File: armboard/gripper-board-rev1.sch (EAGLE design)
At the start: 8 parts

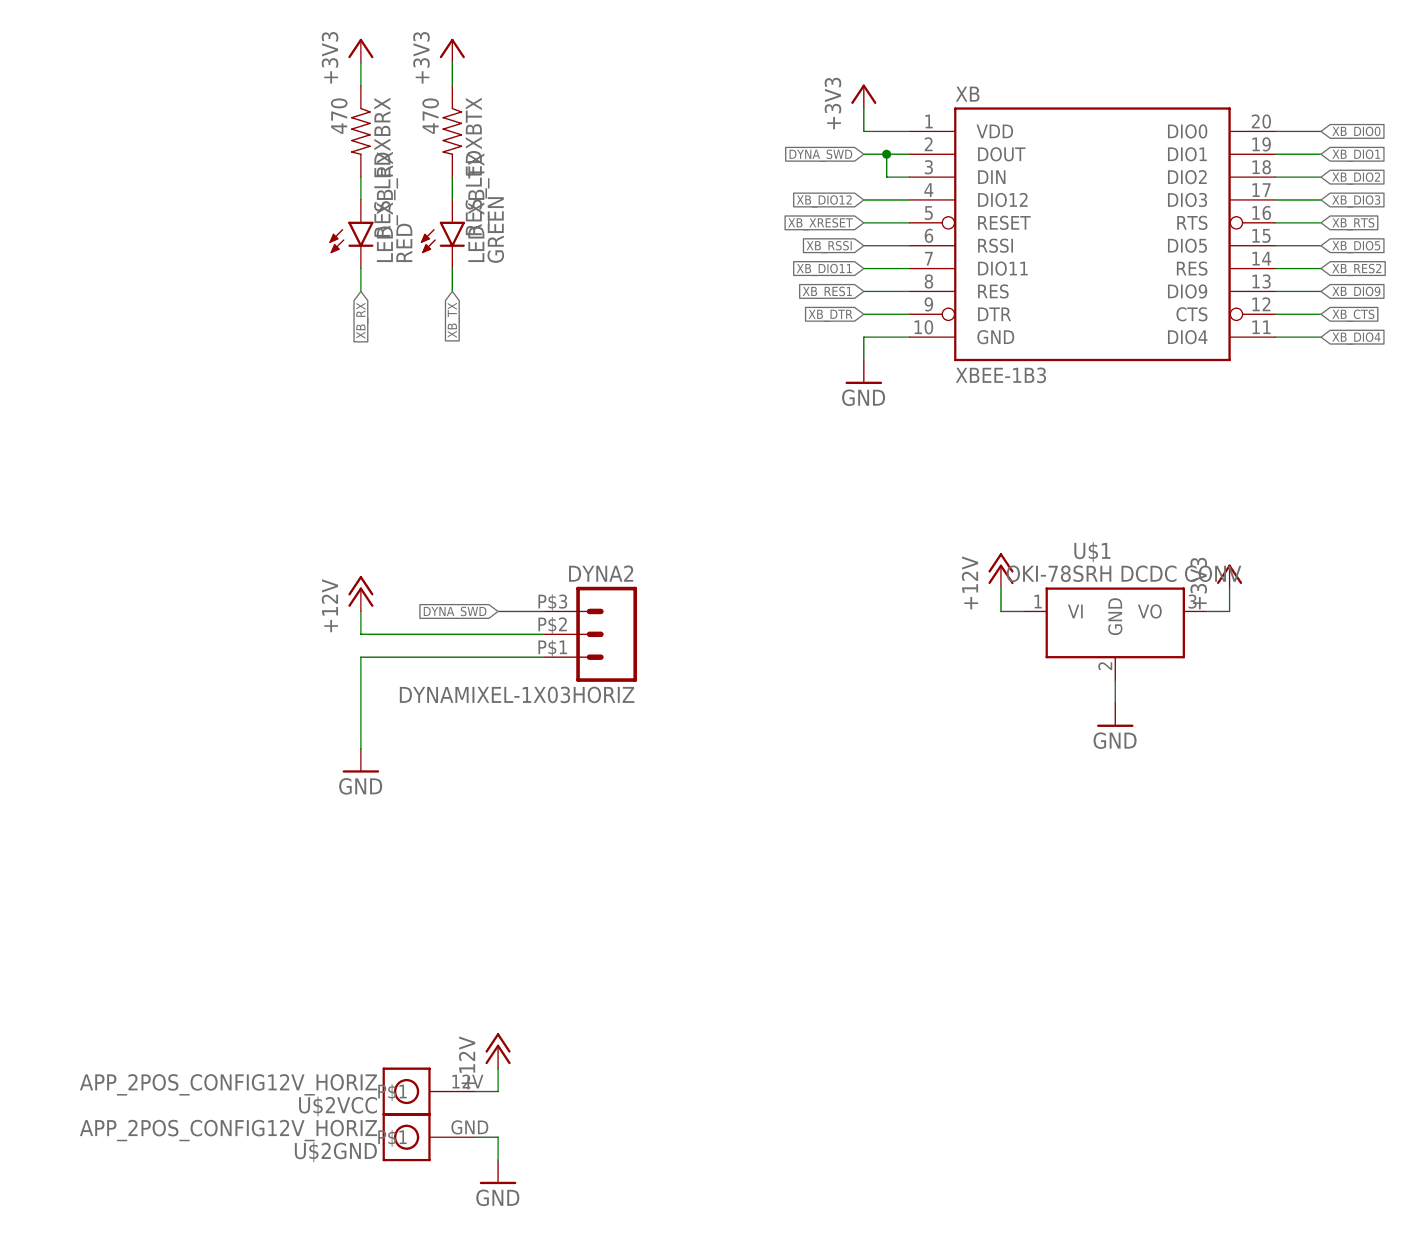
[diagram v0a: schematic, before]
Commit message: moved xbee in a little, reviewed by Drue on arm ; REV 1 FINAL of Gripper Board
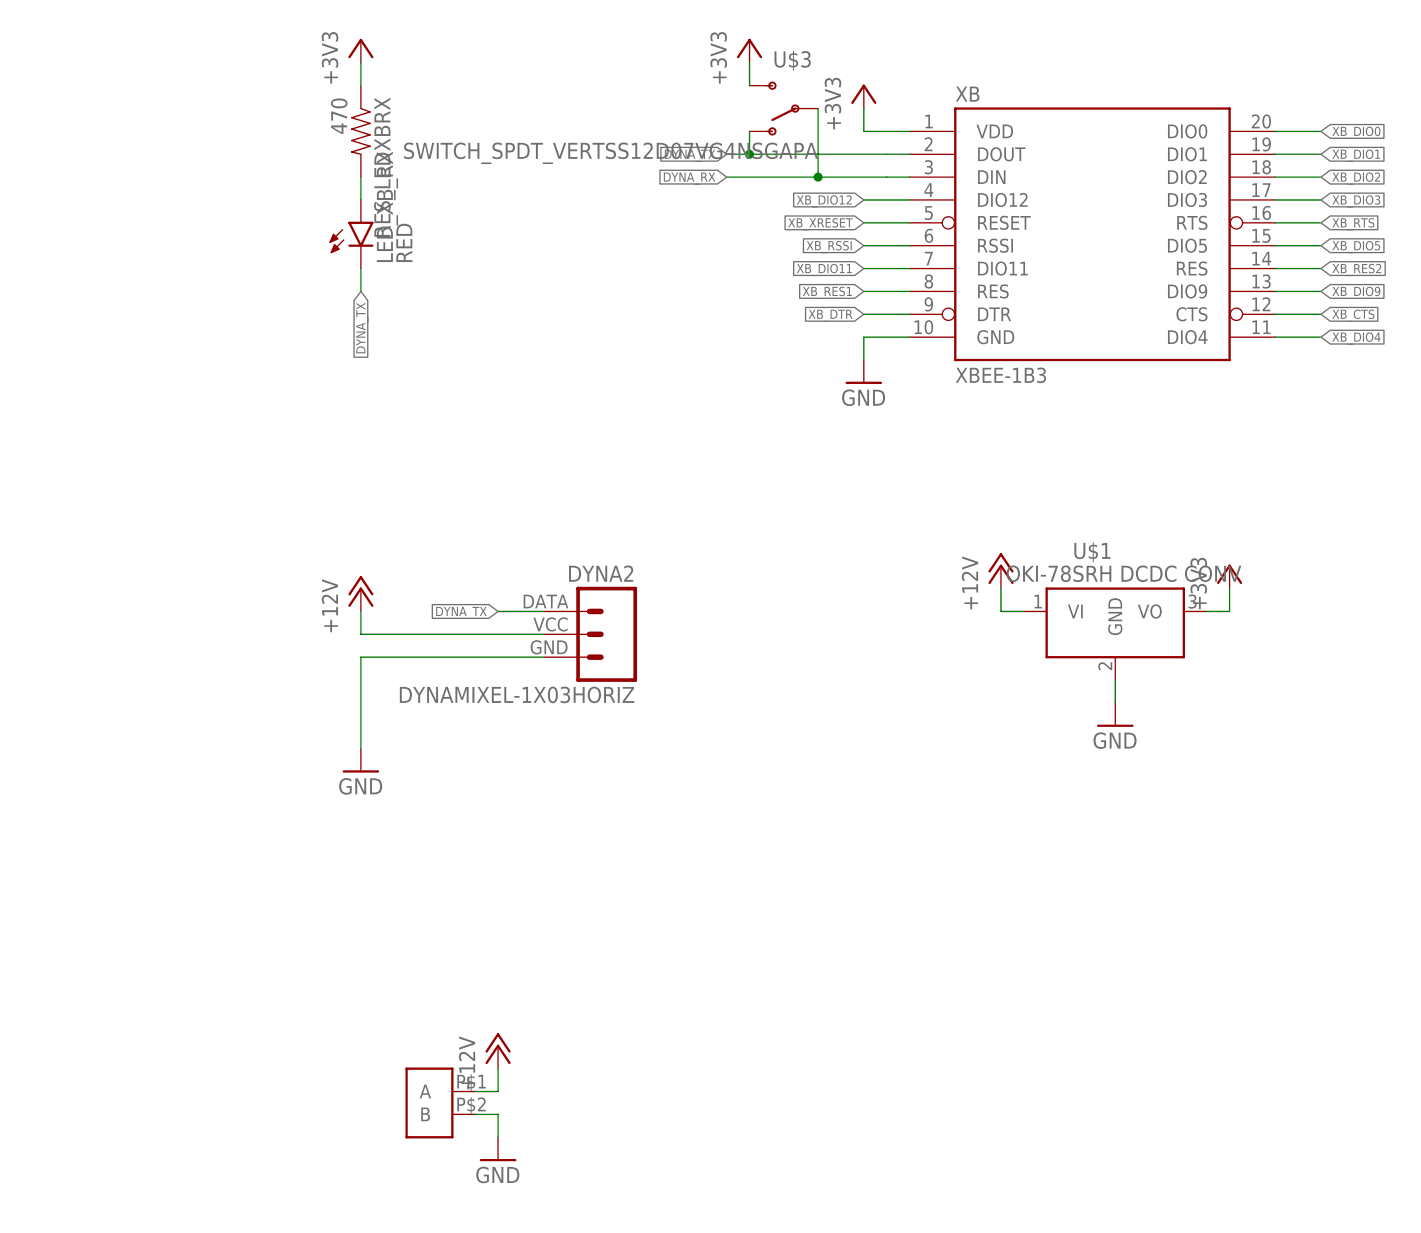
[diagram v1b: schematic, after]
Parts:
- removed LED_XB_TX: GREEN, SparkFun-LED:LED-GREEN1206
- removed RES_LEDXBTX: 470, SparkFun-Passives:RESISTOR1206
- added U$3: SWITCH_SPDT_VERTSS12D07VG4NSGAPA, MRDT-Electromechanical:SWITCH_SPDT_VERTSS12D07VG4NSGAPA
- U$2: value APP_2POS_CONFIG12V_HORIZ -> 2POS_TERM_BLOCKPHOENIX-1935161; device MRDT-Connectors:APP_2POS_CONFIG12V_HORIZ -> MRDT-2015-General:2POS_TERM_BLOCKPHOENIX-1935161
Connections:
- removed net DYNA_SWD: DYNA2.3, XB.DIN, XB.DOUT
- removed net N$2: LED_XB_TX.A, RES_LEDXBTX.2
- removed net XB_RX: LED_XB_RX.C
- removed net XB_TX: LED_XB_TX.C
- new net DYNA_RX: U$3.P, XB.DIN
- new net DYNA_TX: DYNA2.DATA, LED_XB_RX.C, U$3.O, XB.DOUT
- net +12V: now also DYNA2.VCC, U$2.A; no longer DYNA2.2, U$2VCC.P$1
- net +3V3: now also U$3.S; no longer RES_LEDXBTX.1
- net GND: now also DYNA2.GND, U$2.B; no longer DYNA2.1, U$2GND.P$1
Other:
- moved on the sheet: DYNA2
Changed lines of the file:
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@@
 <parts>
 <part name="LED_XB_RX" library="SparkFun-LED" deviceset="LED" device="1206" value="RED"/>
-<part name="LED_XB_TX" library="SparkFun-LED" deviceset="LED-GREEN" device="1206" value="GREEN"/>
 <part name="RES_LEDXBRX" library="SparkFun-Passives" deviceset="RESISTOR" device="1206" value="470"/>
-<part name="RES_LEDXBTX" library="SparkFun-Passives" deviceset="RESISTOR" device="1206" value="470"/>
 <part name="XB" library="SparkFun" deviceset="XBEE-1" device="B3"/>
 <part name="+3V3" library="supply1" deviceset="+3V3" device=""/>
-<part name="+3V4" library="supply1" deviceset="+3V3" device=""/>
 <part name="+3V5" library="supply1" deviceset="+3V3" device=""/>
 <part name="GND14" library="SparkFun" deviceset="GND" device=""/>
@@
 <part name="P+2" library="supply1" deviceset="+12V" device=""/>
 <part name="+3V1" library="supply1" deviceset="+3V3" device=""/>
-<part name="U$2" library="MRDT-Connectors" deviceset="APP_2POS_CONFIG" device="12V_HORIZ"/>
 <part name="GND2" library="SparkFun-Aesthetics" deviceset="GND" device=""/>
 <part name="P+3" library="supply1" deviceset="+12V" device=""/>
+<part name="U$3" library="MRDT-Electromechanical" deviceset="SWITCH_SPDT_VERT" device="SS12D07VG4NSGAPA"/>
+<part name="+3V2" library="supply1" deviceset="+3V3" device=""/>
+<part name="U$2" library="MRDT-2015-General" deviceset="2POS_TERM_BLOCK" device="PHOENIX-1935161"/>
 </parts>
 <sheets>
@@
 <instances>
 <instance part="LED_XB_RX" gate="G$1" x="-17.78" y="22.86"/>
-<instance part="LED_XB_TX" gate="G$1" x="-7.62" y="22.86"/>
 <instance part="RES_LEDXBRX" gate="G$1" x="-17.78" y="33.02" rot="R270"/>
-<instance part="RES_LEDXBTX" gate="G$1" x="-7.62" y="33.02" rot="R270"/>
 <instance part="XB" gate="G$1" x="63.5" y="22.86"/>
 <instance part="+3V3" gate="G$1" x="-17.78" y="43.18"/>
-<instance part="+3V4" gate="G$1" x="-7.62" y="43.18"/>
 <instance part="+3V5" gate="G$1" x="38.1" y="38.1"/>
 <instance part="GND14" gate="1" x="38.1" y="5.08"/>
@@
 <instance part="P+2" gate="1" x="53.34" y="-15.24"/>
 <instance part="+3V1" gate="G$1" x="78.74" y="-15.24"/>
-<instance part="U$2" gate="GND" x="-12.7" y="-78.74" rot="R180"/>
-<instance part="U$2" gate="VCC" x="-12.7" y="-73.66" rot="R180"/>
-<instance part="GND2" gate="1" x="-2.54" y="-83.82"/>
+<instance part="GND2" gate="1" x="-2.54" y="-81.28"/>
 <instance part="P+3" gate="1" x="-2.54" y="-68.58"/>
+<instance part="U$3" gate="G$1" x="30.48" y="35.56" rot="R180"/>
+<instance part="+3V2" gate="G$1" x="25.4" y="43.18"/>
+<instance part="U$2" gate="G$1" x="-12.7" y="-78.74"/>
 </instances>
 <busses>
@@
 </segment>
 <segment>
-<pinref part="DYNA2" gate="G$1" pin="1"/>
+<pinref part="DYNA2" gate="G$1" pin="GND"/>
 <wire x1="2.54" y1="-25.4" x2="-17.78" y2="-25.4" width="0.1524" layer="91"/>
 <wire x1="-17.78" y1="-25.4" x2="-17.78" y2="-35.56" width="0.1524" layer="91"/>
@@
 </segment>
 <segment>
-<pinref part="U$2" gate="GND" pin="P$1"/>
 <pinref part="GND2" gate="1" pin="GND"/>
-<wire x1="-5.08" y1="-78.74" x2="-2.54" y2="-78.74" width="0.1524" layer="91"/>
-<wire x1="-2.54" y1="-78.74" x2="-2.54" y2="-81.28" width="0.1524" layer="91"/>
+<wire x1="-2.54" y1="-76.2" x2="-2.54" y2="-78.74" width="0.1524" layer="91"/>
+<pinref part="U$2" gate="G$1" pin="B"/>
+<wire x1="-2.54" y1="-76.2" x2="-5.08" y2="-76.2" width="0.1524" layer="91"/>
 </segment>
 </net>
@@
 <pinref part="LED_XB_RX" gate="G$1" pin="A"/>
 <pinref part="RES_LEDXBRX" gate="G$1" pin="2"/>
-</segment>
-</net>
-<net name="N$2" class="0">
-<segment>
-<wire x1="-7.62" y1="27.94" x2="-7.62" y2="25.4" width="0.1524" layer="91"/>
-<pinref part="LED_XB_TX" gate="G$1" pin="A"/>
-<pinref part="RES_LEDXBTX" gate="G$1" pin="2"/>
 </segment>
 </net>
@@
 </segment>
 <segment>
-<pinref part="+3V4" gate="G$1" pin="+3V3"/>
-<pinref part="RES_LEDXBTX" gate="G$1" pin="1"/>
-<wire x1="-7.62" y1="40.64" x2="-7.62" y2="38.1" width="0.1524" layer="91"/>
-</segment>
-<segment>
 <pinref part="U$1" gate="G$1" pin="VO"/>
 <wire x1="76.2" y1="-20.32" x2="78.74" y2="-20.32" width="0.1524" layer="91"/>
@@
 <pinref part="+3V1" gate="G$1" pin="+3V3"/>
 </segment>
+<segment>
+<pinref part="U$3" gate="G$1" pin="S"/>
+<pinref part="+3V2" gate="G$1" pin="+3V3"/>
+<wire x1="25.4" y1="40.64" x2="25.4" y2="38.1" width="0.1524" layer="91"/>
+</segment>
 </net>
 <net name="XB_XRESET" class="0">
@@
 </segment>
 </net>
-<net name="XB_RX" class="0">
-<segment>
-<wire x1="-17.78" y1="17.78" x2="-17.78" y2="15.24" width="0.1524" layer="91"/>
-<pinref part="LED_XB_RX" gate="G$1" pin="C"/>
-<label x="-17.78" y="15.24" size="1.016" layer="95" rot="R270" xref="yes"/>
-</segment>
-</net>
-<net name="XB_TX" class="0">
-<segment>
-<wire x1="-7.62" y1="17.78" x2="-7.62" y2="15.24" width="0.1524" layer="91"/>
-<pinref part="LED_XB_TX" gate="G$1" pin="C"/>
-<label x="-7.62" y="15.24" size="1.016" layer="95" rot="R270" xref="yes"/>
-</segment>
-</net>
 <net name="+12V" class="0">
 <segment>
-<pinref part="DYNA2" gate="G$1" pin="2"/>
+<pinref part="DYNA2" gate="G$1" pin="VCC"/>
 <wire x1="2.54" y1="-22.86" x2="-17.78" y2="-22.86" width="0.1524" layer="91"/>
 <wire x1="-17.78" y1="-22.86" x2="-17.78" y2="-20.32" width="0.1524" layer="91"/>
@@
 </segment>
 <segment>
-<pinref part="U$2" gate="VCC" pin="P$1"/>
 <pinref part="P+3" gate="1" pin="+12V"/>
-<wire x1="-5.08" y1="-73.66" x2="-2.54" y2="-73.66" width="0.1524" layer="91"/>
 <wire x1="-2.54" y1="-73.66" x2="-2.54" y2="-71.12" width="0.1524" layer="91"/>
-</segment>
-</net>
-<net name="DYNA_SWD" class="0">
-<segment>
-<pinref part="DYNA2" gate="G$1" pin="3"/>
+<pinref part="U$2" gate="G$1" pin="A"/>
+<wire x1="-2.54" y1="-73.66" x2="-5.08" y2="-73.66" width="0.1524" layer="91"/>
+</segment>
+</net>
+<net name="DYNA_RX" class="0">
+<segment>
+<label x="22.86" y="27.94" size="1.016" layer="95" rot="R180" xref="yes"/>
+<pinref part="U$3" gate="G$1" pin="P"/>
+<wire x1="40.64" y1="27.94" x2="33.02" y2="27.94" width="0.1524" layer="91"/>
+<wire x1="33.02" y1="27.94" x2="22.86" y2="27.94" width="0.1524" layer="91"/>
+<junction x="33.02" y="27.94"/>
+<wire x1="33.02" y1="27.94" x2="33.02" y2="35.56" width="0.1524" layer="91"/>
+<pinref part="XB" gate="G$1" pin="DIN"/>
+<wire x1="40.64" y1="27.94" x2="43.18" y2="27.94" width="0.1524" layer="91"/>
+</segment>
+</net>
+<net name="DYNA_TX" class="0">
+<segment>
+<label x="22.86" y="30.48" size="1.016" layer="95" rot="R180" xref="yes"/>
+<pinref part="U$3" gate="G$1" pin="O"/>
+<wire x1="40.64" y1="30.48" x2="25.4" y2="30.48" width="0.1524" layer="91"/>
+<wire x1="25.4" y1="30.48" x2="22.86" y2="30.48" width="0.1524" layer="91"/>
+<junction x="25.4" y="30.48"/>
+<wire x1="25.4" y1="30.48" x2="25.4" y2="33.02" width="0.1524" layer="91"/>
+<pinref part="XB" gate="G$1" pin="DOUT"/>
+<wire x1="40.64" y1="30.48" x2="43.18" y2="30.48" width="0.1524" layer="91"/>
+</segment>
+<segment>
+<pinref part="DYNA2" gate="G$1" pin="DATA"/>
 <label x="-2.54" y="-20.32" size="1.016" layer="95" rot="R180" xref="yes"/>
 <wire x1="2.54" y1="-20.32" x2="-2.54" y2="-20.32" width="0.1524" layer="91"/>
 </segment>
 <segment>
-<pinref part="XB" gate="G$1" pin="DIN"/>
-<wire x1="43.18" y1="27.94" x2="40.64" y2="27.94" width="0.1524" layer="91"/>
-<pinref part="XB" gate="G$1" pin="DOUT"/>
-<wire x1="43.18" y1="30.48" x2="40.64" y2="30.48" width="0.1524" layer="91"/>
-<label x="38.1" y="30.48" size="1.016" layer="95" rot="R180" xref="yes"/>
-<wire x1="40.64" y1="30.48" x2="38.1" y2="30.48" width="0.1524" layer="91"/>
-<wire x1="40.64" y1="27.94" x2="40.64" y2="30.48" width="0.1524" layer="91"/>
-<junction x="40.64" y="30.48"/>
-</segment>
-</net>
+<wire x1="-17.78" y1="17.78" x2="-17.78" y2="15.24" width="0.1524" layer="91"/>
+<pinref part="LED_XB_RX" gate="G$1" pin="C"/>
+<label x="-17.78" y="15.24" size="1.016" layer="95" rot="R270" xref="yes"/>
+</segment>
+</net>
